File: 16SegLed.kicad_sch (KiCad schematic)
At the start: 33 parts, among them J1 Conn_01x10, J2 Conn_01x10, J3 Conn_01x10, J4 Conn_01x06_Socket, J5 Conn_01x04_Pin, J6 Conn_01x04_Pin, SW1 SW_Push, SW2 SW_Push, U1 ESP32-S3-WROOM-1, U2 AMS1117-3.3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

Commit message: Update USB connectors to be able to move I2C 5V test connector to less crowded place
- using 2 of them (support installation on front and back in parallel in case needed differently in application than in prototype)
- using own footprint, matching LCSC part C5342444
- including own 3d model
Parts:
- added USB1: JST-PH2.0-4P, ProjectLibrary:PH 1x04 P2.0, symbol Connector:Conn_01x04_Pin
- USB1: footprint Connector_JST:JST_PH_S4B-PH-K_1x04_P2.00mm_Horizontal -> ProjectLibrary:PH 1x04 P2.0; LCSC (none) -> C5342444
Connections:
- net +5V: now also USB1.4 (Pin_4)
- net GND: now also USB1.1 (Pin_1)
- net USB_D_MINUS: now also USB1.3 (Pin_3)
- net USB_D_PLUS: now also USB1.2 (Pin_2)
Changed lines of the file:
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@@
+    (effects (font (size 1.27 1.27)) (justify left bottom))
+  )
+  (label "USB_D_PLUS" (at 142.875 135.89 0) (fields_autoplaced)
     (effects (font (size 1.27 1.27)) (justify left bottom))
   )
@@
   )
   (label "IO13" (at 216.535 107.315 0) (fields_autoplaced)
+    (effects (font (size 1.27 1.27)) (justify left bottom))
+  )
+  (label "USB_D_MINUS" (at 142.875 133.35 0) (fields_autoplaced)
     (effects (font (size 1.27 1.27)) (justify left bottom))
   )
@@
     )
   )
+  (symbol (lib_id "power:GND") (at 142.875 138.43 0) (unit 1)
+    (in_bom yes) (on_board yes) (dnp no) (fields_autoplaced)
+    (property "Reference" "#PWR02" (at 142.875 144.78 0)
+      (effects (font (size 1.27 1.27)) hide)
+    )
+    (property "Value" "GND" (at 142.875 143.51 0)
+      (effects (font (size 1.27 1.27)))
+    )
+    (property "Footprint" "" (at 142.875 138.43 0)
+      (effects (font (size 1.27 1.27)) hide)
+    )
+    (property "Datasheet" "" (at 142.875 138.43 0)
+      (effects (font (size 1.27 1.27)) hide)
+    )
+    (pin "1")
+    (instances
+      (project "Kitchen Clock 3"
+        (path "/159f713c-06e7-46f4-875d-049e06e83ded"
+          (reference "#PWR02") (unit 1)
+        )
+      )
+      (project "16SegLed"
+        (path "/41dad044-0879-44f7-af2f-de3faef8859f"
+          (reference "#PWR041") (unit 1)
+        )
+      )
+    )
+  )
   (symbol (lib_id "Device:C_Polarized_Small") (at 208.28 134.62 0) (unit 1)
     (in_bom yes) (on_board yes) (dnp yes)
@@
       (effects (font (size 1.27 1.27)))
     )
-    (property "Footprint" "Connector_JST:JST_PH_S4B-PH-K_1x04_P2.00mm_Horizontal" (at 162.56 135.89 0)
-      (effects (font (size 1.27 1.27)) hide)
-    )
-    (property "Datasheet" "~" (at 162.56 135.89 0)
+    (property "Footprint" "ProjectLibrary:PH 1x04 P2.0" (at 162.56 135.89 0)
+      (effects (font (size 1.27 1.27)) hide)
+    )
+    (property "Datasheet" "https://datasheet.lcsc.com/lcsc/2307071616_HCTL-HC-PH-4AW-G_C5342444.pdf" (at 162.56 135.89 0)
+      (effects (font (size 1.27 1.27)) hide)
+    )
+    (property "LCSC" "C5342444" (at 162.56 135.89 0)
       (effects (font (size 1.27 1.27)) hide)
     )
@@
         (path "/41dad044-0879-44f7-af2f-de3faef8859f"
           (reference "USB1") (unit 1)
+        )
+      )
+    )
+  )
+  (symbol (lib_id "power:+5V") (at 142.875 130.81 0) (unit 1)
+    (in_bom yes) (on_board yes) (dnp no) (fields_autoplaced)
+    (property "Reference" "#PWR05" (at 142.875 134.62 0)
+      (effects (font (size 1.27 1.27)) hide)
+    )
+    (property "Value" "+5V" (at 142.875 127 0)
+      (effects (font (size 1.27 1.27)))
+    )
+    (property "Footprint" "" (at 142.875 130.81 0)
+      (effects (font (size 1.27 1.27)) hide)
+    )
+    (property "Datasheet" "" (at 142.875 130.81 0)
+      (effects (font (size 1.27 1.27)) hide)
+    )
+    (pin "1")
+    (instances
+      (project "Kitchen Clock 3"
+        (path "/159f713c-06e7-46f4-875d-049e06e83ded"
+          (reference "#PWR05") (unit 1)
+        )
+      )
+      (project "16SegLed"
+        (path "/41dad044-0879-44f7-af2f-de3faef8859f"
+          (reference "#PWR042") (unit 1)
         )
       )
@@
         )
       )
+    )
+  )
+  (symbol (lib_id "Connector:Conn_01x04_Pin") (at 137.795 135.89 0) (mirror x) (unit 1)
+    (in_bom yes) (on_board yes) (dnp yes)
+    (property "Reference" "USB1" (at 138.43 142.24 0)
+      (effects (font (size 1.27 1.27)))
+    )
+    (property "Value" "JST-PH2.0-4P" (at 137.795 139.7 0)
+      (effects (font (size 1.27 1.27)))
+    )
+    (property "Footprint" "ProjectLibrary:PH 1x04 P2.0" (at 137.795 135.89 0)
+      (effects (font (size 1.27 1.27)) hide)
+    )
+    (property "Datasheet" "https://datasheet.lcsc.com/lcsc/2307071616_HCTL-HC-PH-4AW-G_C5342444.pdf" (at 137.795 135.89 0)
+      (effects (font (size 1.27 1.27)) hide)
+    )
+    (property "LCSC" "C5342444" (at 137.795 135.89 0)
+      (effects (font (size 1.27 1.27)) hide)
+    )
+    (pin "1")
+    (pin "2")
+    (pin "3")
+    (pin "4")
+    (instances
+      (project "Kitchen Clock 3"
+        (path "/159f713c-06e7-46f4-875d-049e06e83ded"
+          (reference "USB1") (unit 1)
+        )
+      )
+      (project "16SegLed"
+        (path "/41dad044-0879-44f7-af2f-de3faef8859f"
+          (reference "USB2") (unit 1)
+        )
+      )

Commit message: Reset usage of flag "do not place"
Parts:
- C1, C10, C11, C2, C4, C5, C9, J4, J5, J6, R1, R13, SW1, SW2, U1, U2, U5, USB1: now fitted
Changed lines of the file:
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@@
   )
   (symbol (lib_id "Connector:Conn_01x04_Pin") (at 146.685 178.435 0) (mirror x) (unit 1)
-    (in_bom yes) (on_board yes) (dnp yes)
+    (in_bom yes) (on_board yes) (dnp no)
     (property "Reference" "J6" (at 147.32 185.42 0)
       (effects (font (size 1.27 1.27)))
@@
   )
   (symbol (lib_id "Connector:Conn_01x06_Socket") (at 207.01 102.235 0) (mirror y) (unit 1)
-    (in_bom yes) (on_board yes) (dnp yes)
+    (in_bom yes) (on_board yes) (dnp no)
     (property "Reference" "J4" (at 205.105 103.505 90)
       (effects (font (size 1.27 1.27)))
@@
   )
   (symbol (lib_id "Connector:Conn_01x04_Pin") (at 116.205 178.435 0) (mirror x) (unit 1)
-    (in_bom yes) (on_board yes) (dnp yes)
+    (in_bom yes) (on_board yes) (dnp no)
     (property "Reference" "J5" (at 116.84 185.42 0)
       (effects (font (size 1.27 1.27)))
@@
   )
   (symbol (lib_id "Device:C_Polarized_Small") (at 208.28 134.62 0) (unit 1)
-    (in_bom yes) (on_board yes) (dnp yes)
+    (in_bom yes) (on_board yes) (dnp no)
     (property "Reference" "C9" (at 210.82 133.4389 0)
       (effects (font (size 1.27 1.27)) (justify left))
@@
   )
   (symbol (lib_id "Device:C_Polarized_Small") (at 238.125 137.795 0) (unit 1)
-    (in_bom yes) (on_board yes) (dnp yes) (fields_autoplaced)
+    (in_bom yes) (on_board yes) (dnp no) (fields_autoplaced)
     (property "Reference" "C4" (at 241.3 135.9789 0)
       (effects (font (size 1.27 1.27)) (justify left))
@@
   )
   (symbol (lib_id "Connector:Conn_01x04_Pin") (at 162.56 135.89 0) (mirror x) (unit 1)
-    (in_bom yes) (on_board yes) (dnp yes)
+    (in_bom yes) (on_board yes) (dnp no)
     (property "Reference" "USB1" (at 163.195 142.24 0)
       (effects (font (size 1.27 1.27)))
@@
   )
   (symbol (lib_id "Switch:SW_Push") (at 203.2 55.245 0) (unit 1)
-    (in_bom yes) (on_board yes) (dnp yes)
+    (in_bom yes) (on_board yes) (dnp no)
     (property "Reference" "SW2" (at 203.2 59.055 0)
       (effects (font (size 1.27 1.27)))
@@
   )
   (symbol (lib_id "Switch:SW_Push") (at 45.085 47.625 90) (unit 1)
-    (in_bom yes) (on_board yes) (dnp yes) (fields_autoplaced)
+    (in_bom yes) (on_board yes) (dnp no) (fields_autoplaced)
     (property "Reference" "SW1" (at 46.99 46.355 90)
       (effects (font (size 1.27 1.27)) (justify right))
@@
   )
   (symbol (lib_id "Regulator_Linear:AMS1117-3.3") (at 252.73 130.175 0) (unit 1)
-    (in_bom yes) (on_board yes) (dnp yes) (fields_autoplaced)
+    (in_bom yes) (on_board yes) (dnp no) (fields_autoplaced)
     (property "Reference" "U2" (at 252.73 123.19 0)
       (effects (font (size 1.27 1.27)))
@@
   )
   (symbol (lib_id "Power_Protection:SRV05-4") (at 34.29 85.725 0) (unit 1)
-    (in_bom yes) (on_board yes) (dnp yes) (fields_autoplaced)
+    (in_bom yes) (on_board yes) (dnp no) (fields_autoplaced)
     (property "Reference" "U5" (at 37.9161 71.12 0)
       (effects (font (size 1.27 1.27)) (justify left))
@@
   )
   (symbol (lib_id "Device:C_Small") (at 233.045 137.795 0) (mirror x) (unit 1)
-    (in_bom yes) (on_board yes) (dnp yes)
+    (in_bom yes) (on_board yes) (dnp no)
     (property "Reference" "C11" (at 229.87 136.5186 0)
       (effects (font (size 1.27 1.27)) (justify right))
@@
   )
   (symbol (lib_id "PCM_Espressif:ESP32-S3-WROOM-1") (at 111.125 75.565 0) (unit 1)
-    (in_bom yes) (on_board yes) (dnp yes)
+    (in_bom yes) (on_board yes) (dnp no)
     (property "Reference" "U1" (at 113.3191 33.02 0)
       (effects (font (size 1.27 1.27)) (justify left))
@@
   )
   (symbol (lib_id "Device:C_Small") (at 119.38 26.035 90) (unit 1)
-    (in_bom yes) (on_board yes) (dnp yes) (fields_autoplaced)
+    (in_bom yes) (on_board yes) (dnp no) (fields_autoplaced)
     (property "Reference" "C2" (at 119.3863 19.685 90)
       (effects (font (size 1.27 1.27)))
@@
   )
   (symbol (lib_id "Device:C_Polarized_Small") (at 266.065 137.795 0) (mirror y) (unit 1)
-    (in_bom yes) (on_board yes) (dnp yes)
+    (in_bom yes) (on_board yes) (dnp no)
     (property "Reference" "C5" (at 262.89 135.9789 0)
       (effects (font (size 1.27 1.27)) (justify left))
@@
   )
   (symbol (lib_id "Device:R_Small") (at 175.26 -14.605 0) (unit 1)
-    (in_bom yes) (on_board yes) (dnp yes)
+    (in_bom yes) (on_board yes) (dnp no)
     (property "Reference" "R13" (at 177.165 -15.875 0)
       (effects (font (size 1.27 1.27)) (justify left))
@@
   )
   (symbol (lib_id "Device:C_Small") (at 271.145 137.795 180) (unit 1)
-    (in_bom yes) (on_board yes) (dnp yes)
+    (in_bom yes) (on_board yes) (dnp no)
     (property "Reference" "C10" (at 274.32 136.5186 0)
       (effects (font (size 1.27 1.27)) (justify right))
@@
   )
   (symbol (lib_id "Device:C_Small") (at 27.94 43.18 0) (unit 1)
-    (in_bom yes) (on_board yes) (dnp yes) (fields_autoplaced)
+    (in_bom yes) (on_board yes) (dnp no) (fields_autoplaced)
     (property "Reference" "C1" (at 31.115 41.9163 0)
       (effects (font (size 1.27 1.27)) (justify left))
@@
   )
   (symbol (lib_id "Device:R_Small") (at 27.94 36.83 0) (unit 1)
-    (in_bom yes) (on_board yes) (dnp yes) (fields_autoplaced)
+    (in_bom yes) (on_board yes) (dnp no) (fields_autoplaced)
     (property "Reference" "R1" (at 29.845 35.56 0)
       (effects (font (size 1.27 1.27)) (justify left))
@@
   )
   (symbol (lib_id "Connector:Conn_01x04_Pin") (at 137.795 135.89 0) (mirror x) (unit 1)
-    (in_bom yes) (on_board yes) (dnp yes)
+    (in_bom yes) (on_board yes) (dnp no)
     (property "Reference" "USB1" (at 138.43 142.24 0)
       (effects (font (size 1.27 1.27)))

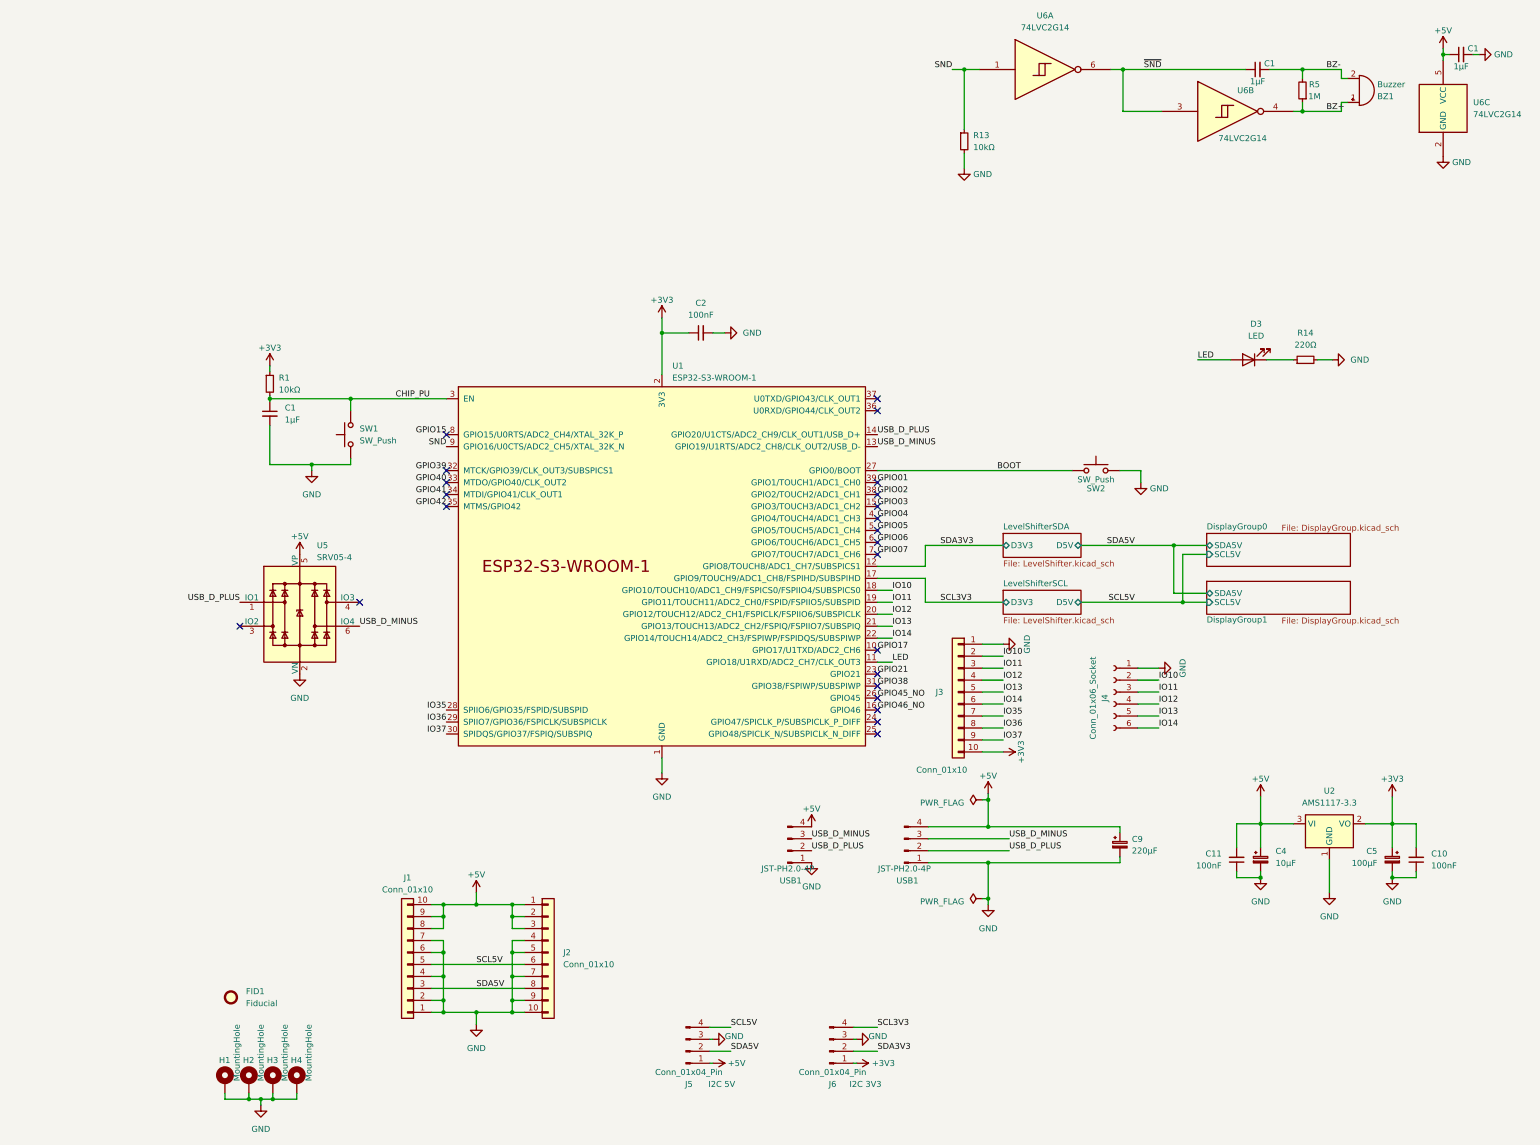
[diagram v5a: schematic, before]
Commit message: Create schematic PDF
- Define and use slim sheet template
- Define sheet values
- Rearrange schematics for printout
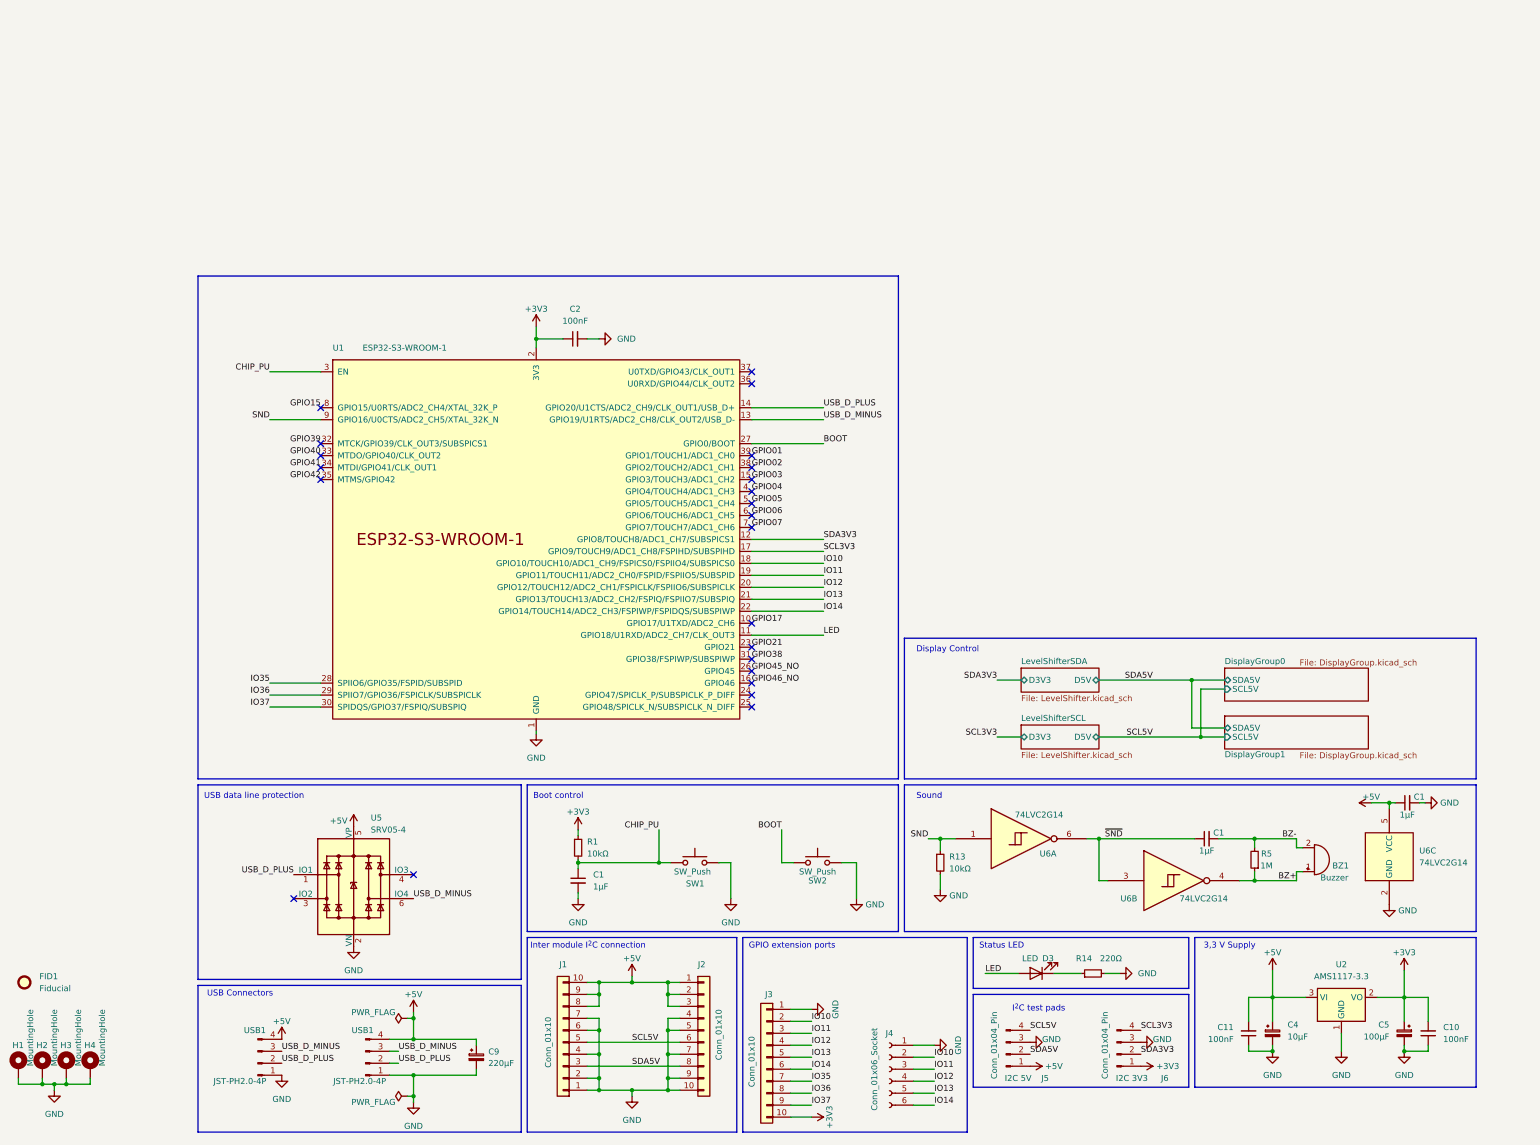
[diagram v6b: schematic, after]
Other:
- note added: "3,3 V Supply"
- note added: "Boot control"
- note added: "Display Control"
- note added: "GPIO extension ports"
- note added: "I^{2}C test pads"
- note added: "Inter module I^{2}C connection"
- note added: "Sound"
- note added: "Status LED"
- note added: "USB Connectors"
- note added: "USB data line protection"
- title: (none) -> 14 Segment Display Module
- moved on the sheet: BZ1, C1, C10, C11, C2, C4, C5, C9, D3, FID1, H1, H2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
